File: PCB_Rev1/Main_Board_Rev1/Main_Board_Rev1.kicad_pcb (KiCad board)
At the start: 4 copper layers, 152.4 x 152.4 mm, 83 parts, among them IC1 LT8648SEV#PBF, J1 PRT-14017, J10 B4B-PH-K-S, J11 532610771, J12 532610771, J13 532610771, J2 Conn_01x04_Socket, J3 691137710002, J4 Conn_01x02_Pin, J5 XT60PW-M, J6 Conn_01x02_Pin, J7 Conn_01x02_Pin, J8 Conn_01x02_Pin, J9 B4B-PH-K-S, Q1 AO3400A, Q2 AO3400A, Q3 AO3400A, Q4 IRFHM9331TRPBF, U1 AZ1117IH-3.3TRG1, U2 L298N, X1 B2P-VH, X2 B2P-VH

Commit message: Added routing
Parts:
- moved LED1 0.93 mm to (97.3, 155.0)
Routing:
- net Ch.A_MOTOR_2: track 0.00 -> 168.4 mm, vias 0 -> 4
- net Ch.B_MOTOR_2: track 0.00 -> 168.0 mm, vias 0 -> 4
- net /CSTAR-Drive/OUT2_MOTOR_1: track 6.11 -> 144.4 mm, vias 0 -> 4
- net /CSTAR-Drive/OUT2_MOTOR_2: track 0.00 -> 98.0 mm, vias 0 -> 4
- net /CSTAR-Drive/OUT1_MOTOR_1: track 0.00 -> 81.1 mm, vias 0 -> 3
- net Ch.B_MOTOR_1: track 0.00 -> 78.8 mm, vias 0 -> 4
- net Ch.A_MOTOR_1: track 0.00 -> 78.5 mm, vias 0 -> 4
- net Net-(IC1-EN/UV): track 0.00 -> 62.1 mm, vias 0 -> 4
- net 24VEXT: track 0.00 -> 49.2 mm, vias 0 -> 4
- net Net-(C1-Pad1): track 0.00 -> 48.4 mm, vias 0 -> 2
- net Net-(J7-Pin_2): track 0.00 -> 41.7 mm, vias 0 -> 4
- net Net-(PS1-FB): track 0.00 -> 39.9 mm, vias 0 -> 4
- net BATT_IN: track 0.00 -> 28.2 mm, vias 0 -> 2
- net Net-(J3-Pad1): track 0.00 -> 27.7 mm
- net Net-(J6-Pin_2): track 0.00 -> 17.0 mm, vias 0 -> 2
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
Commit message: Routing
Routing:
- net RGB_Blue_Control: track 166.5 -> 153.9 mm, vias 4 -> 3
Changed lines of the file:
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@@
 	)
 	(segment
-		(start 146 96.5)
+		(start 146 97)
 		(end 146 122.5)
-		(width 0.2)
-		(layer "F.Cu")
-		(net 34)
-	)
-	(segment
-		(start 167.438 96.622)
-		(end 163.122 96.622)
 		(width 0.2)
 		(layer "F.Cu")
@@
 		(net 34)
 	)
-	(segment
-		(start 163.122 96.622)
-		(end 163 96.5)
-		(width 0.2)
-		(layer "F.Cu")
-		(net 34)
-	)
-	(segment
-		(start 168.5 95.56)
-		(end 167.438 96.622)
-		(width 0.2)
-		(layer "F.Cu")
-		(net 34)
-	)
 	(via
 		(at 146 122.5)
@@
 	)
 	(via
-		(at 146 96.5)
+		(at 146 97)
 		(size 0.6)
 		(drill 0.3)
@@
 	(via
 		(at 42.5 122.5)
-		(size 0.6)
-		(drill 0.3)
-		(layers "F.Cu" "B.Cu")
-		(net 34)
-	)
-	(via
-		(at 163.122 96.622)
 		(size 0.6)
 		(drill 0.3)
@@
 	)
 	(segment
-		(start 163 96.5)
-		(end 163.122 96.622)
+		(start 167.06 97)
+		(end 168.5 95.56)
 		(width 0.2)
 		(layer "B.Cu")
@@
 	)
 	(segment
-		(start 146 96.5)
-		(end 158 96.5)
+		(start 146 97)
+		(end 167.06 97)
 		(width 0.2)
 		(layer "B.Cu")
-		(net 34)
-	)
-	(segment
-		(start 146 96.5)
-		(end 163 96.5)
-		(width 0.2)
-		(layer "B.Cu")

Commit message: Routing
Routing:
- net RGB_Red_Control: track 182.7 -> 180.6 mm, vias 6 -> 5
- net RGB_Green_Control: track 172.0 -> 173.3 mm, vias 6 -> 5
- net Ch.B_MOTOR_2: track 168.0 -> 169.0 mm, vias 4 -> 3
- net GPIO13: track 124.3 -> 123.4 mm, vias 6 -> 5
- net Ch.B_MOTOR_1: track 78.8 -> 79.5 mm, vias 4 -> 3
- net Ch.A_MOTOR_1: track 78.5 -> 78.8 mm, vias 4 -> 3
- net GPIO8: track 76.5 -> 76.4 mm, vias 4 -> 3
- net GPIO7: vias 4 -> 3
- net GPIO2: vias 3 -> 2
- net GPIO12: vias 6 -> 5
- net GPIO0: vias 4 -> 3
- net TXD_LIDAR: vias 4 -> 3
- net RXD_LIDAR: vias 4 -> 3
- net LIDAR_IO: vias 4 -> 3
- net GPIO9: vias 4 -> 3
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
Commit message: Routing
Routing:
- net EN_DRIVER_2: track 0.00 -> 122.2 mm, vias 0 -> 4
- net IN2_DRIVER_2: track 0.00 -> 109.4 mm, vias 0 -> 4
- net IN1_DRIVER_2: track 0.00 -> 109.2 mm, vias 0 -> 4
- net /CSTAR-Drive/OUT2_MOTOR_2: track 98.0 -> 128.0 mm, vias 4 -> 5
- net /CSTAR-Drive/OUT2_MOTOR_1: track 144.4 -> 144.7 mm, vias 4 -> 2
- net /CSTAR-Drive/OUT1_MOTOR_2: vias 8 -> 6

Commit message: some more routing
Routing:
- net +3V3: track 0.00 -> 108.5 mm, vias 0 -> 5
- net GND: track 0.00 -> 68.4 mm, vias 0 -> 3
- net 5VEXT: track 0.00 -> 10.4 mm, vias 0 -> 2
- net Net-(C3-Pad1): track 4.91 -> 5.97 mm, vias 0 -> 2

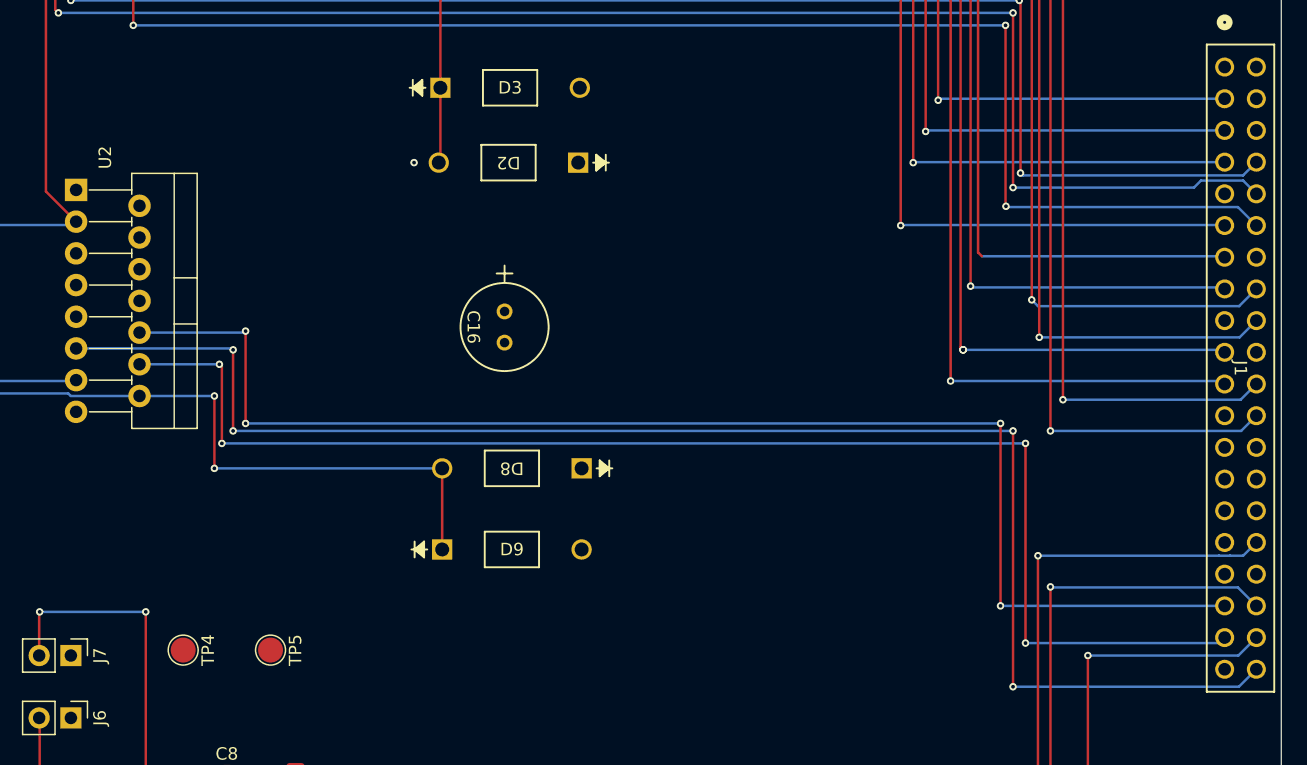
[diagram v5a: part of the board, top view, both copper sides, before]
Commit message: TP for Motor Drive + U2 Routing
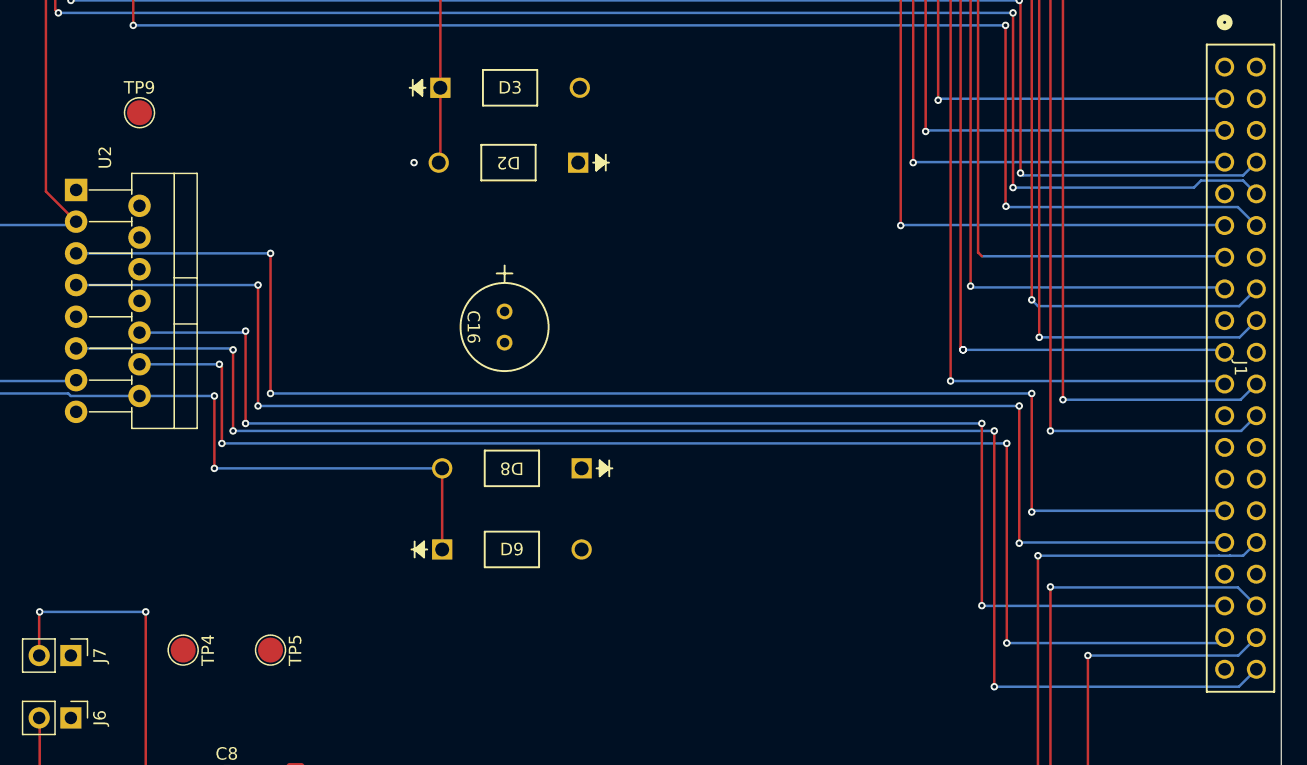
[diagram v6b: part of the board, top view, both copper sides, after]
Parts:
- added TP9: Motor_Out, TestPoint:TestPoint_Pad_D2.0mm, F.Cu at (79.0, 53.5)
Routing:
- net IN1_DRIVER_1: track 0.00 -> 112.8 mm, vias 0 -> 4
- net IN2_DRIVER_1: track 0.00 -> 112.8 mm, vias 0 -> 4

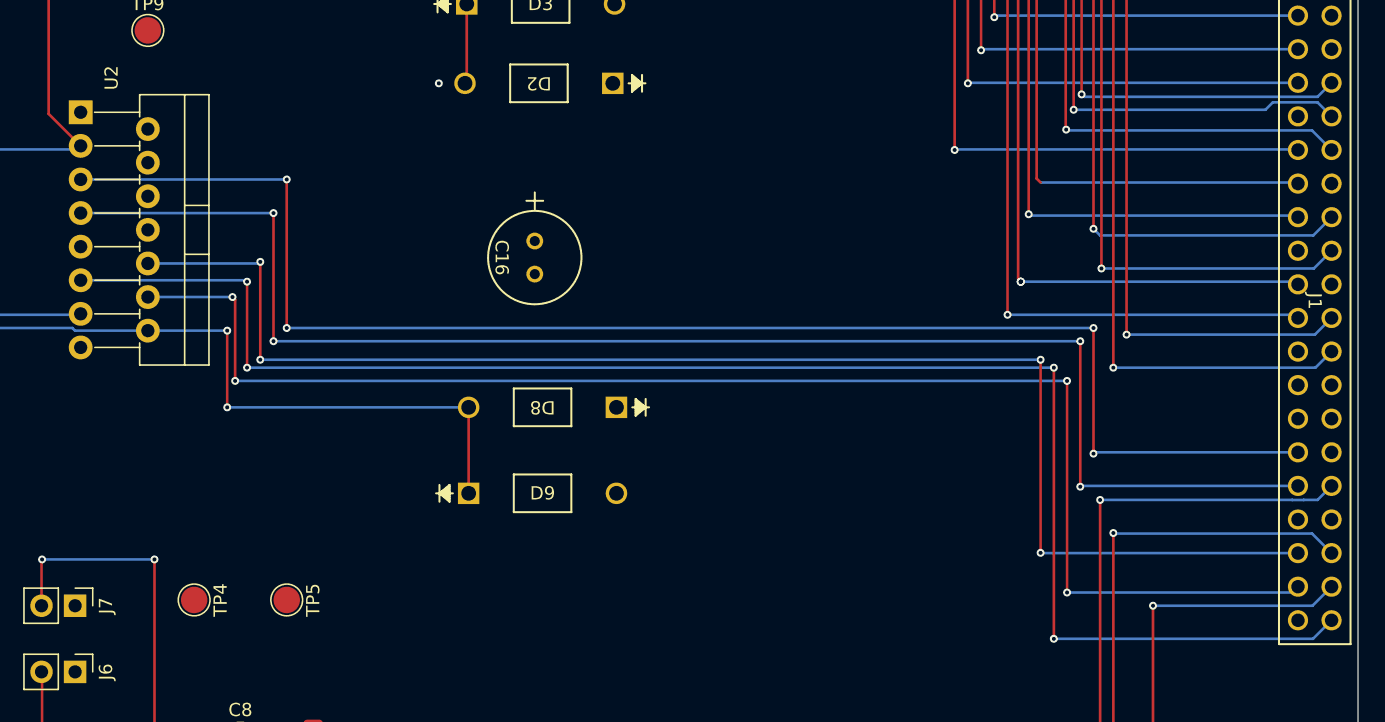
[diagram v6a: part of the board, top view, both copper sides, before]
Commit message: Routing U2 Enable Pin
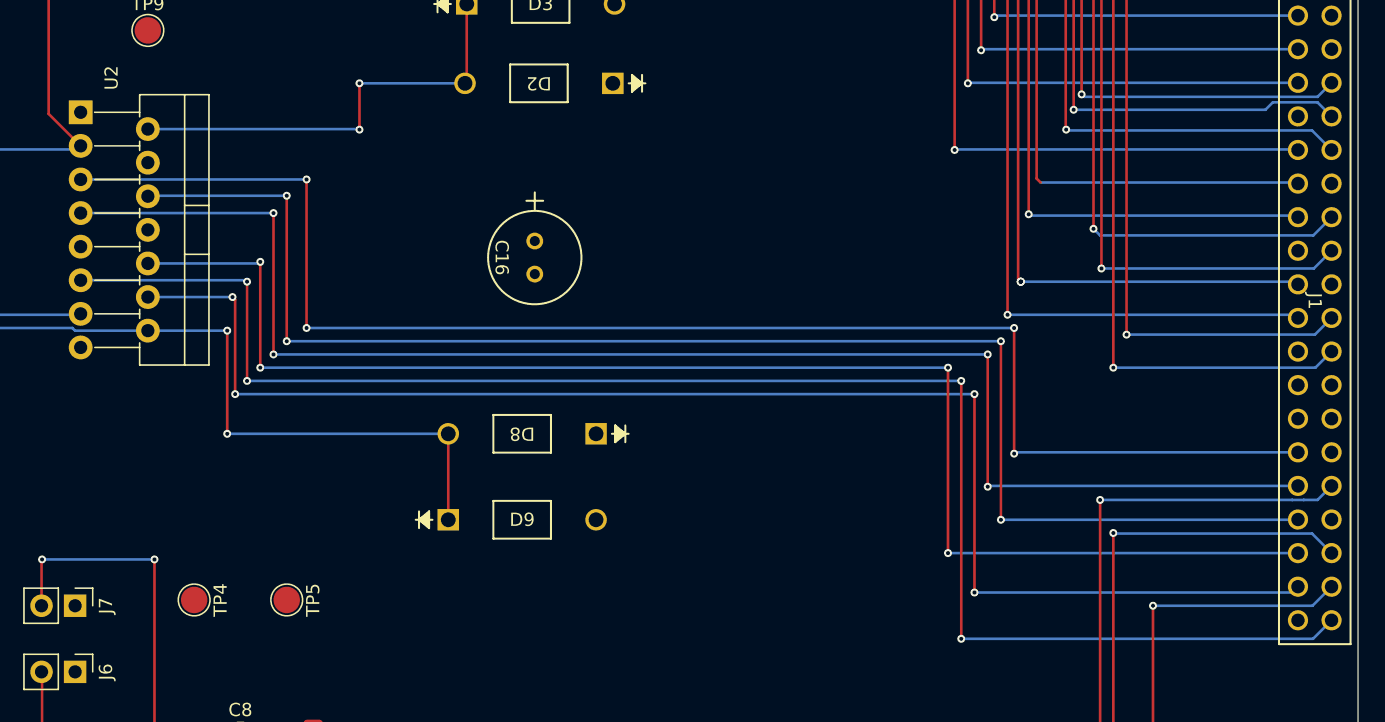
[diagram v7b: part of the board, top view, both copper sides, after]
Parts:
- moved D8 2.53 mm to (112.9, 84.0)
- moved D9 2.53 mm to (101.7, 90.5)
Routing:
- net EN_DRIVER_1: track 0.00 -> 111.5 mm, vias 0 -> 4
- net /CSTAR-Drive/OUT1_MOTOR_1: track 81.1 -> 108.6 mm, vias 3 -> 4

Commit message: More routing
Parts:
- moved C14 10.6 mm to (145.1, 163.9), turned to 0 degrees
- moved C10 7.72 mm to (143.0, 149.6)
- moved C11 7.72 mm to (138.5, 156.5)
- moved C12 7.72 mm to (135.0, 163.5)
- moved F3 7.72 mm to (136.0, 133.0)
- moved J8 7.72 mm to (143.0, 140.0)
- moved L2 7.72 mm to (138.5, 163.5)
- moved LED4 7.72 mm to (129.5, 137.5)
- moved PS1 7.72 mm to (137.3, 149.8)
- moved R12 7.72 mm to (133.5, 143.0)
- moved R13 7.72 mm to (124.3, 142.0)
- moved R11 7.72 mm to (129.5, 132.9)
- moved C13 7.36 mm to (145.1, 158.9), turned to 0 degrees
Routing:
- net 5VEXT: track 10.4 -> 199.6 mm, vias 2 -> 13
- net GND: track 68.4 -> 100.8 mm, vias 3 -> 7
- net 12VEXT: track 0.00 -> 9.67 mm, vias 0 -> 2
- net Net-(J8-Pin_1): track 14.9 -> 17.0 mm, vias 0 -> 2
- net Net-(PS1-SW): track 16.7 -> 16.5 mm, vias 0 -> 2
